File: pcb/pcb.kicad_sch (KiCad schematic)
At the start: 10 parts, among them J1 encoder, J2 programmer, J3 oled display, J4 usb-ttl, SW1 reset, U1 ATmega32-16P

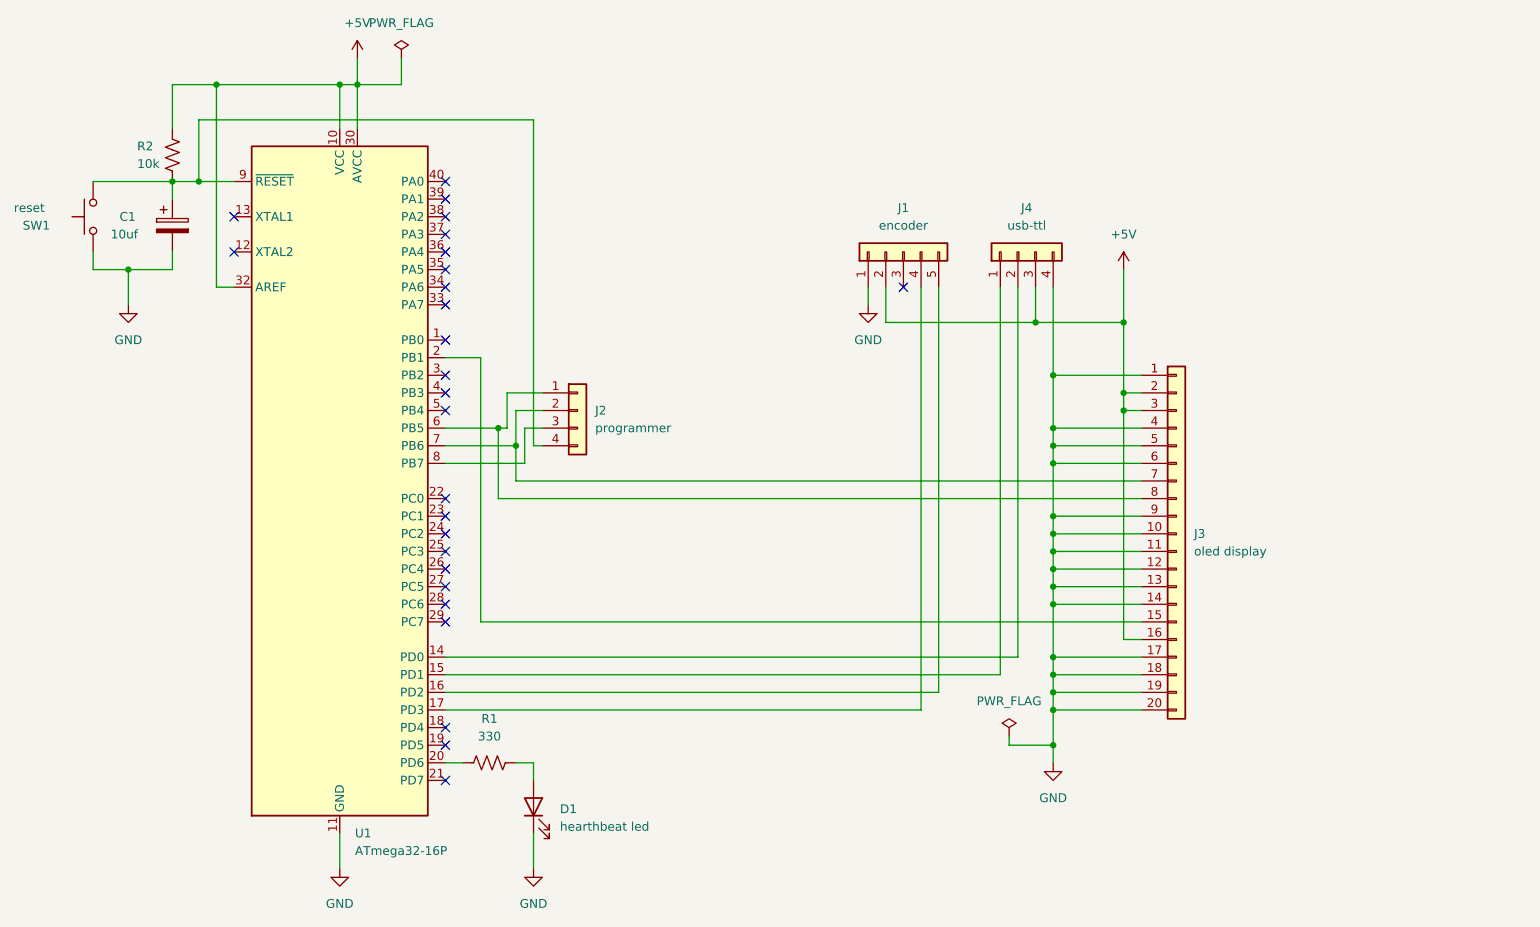
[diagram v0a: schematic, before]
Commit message: actualizo PCB con switches next, prev, play
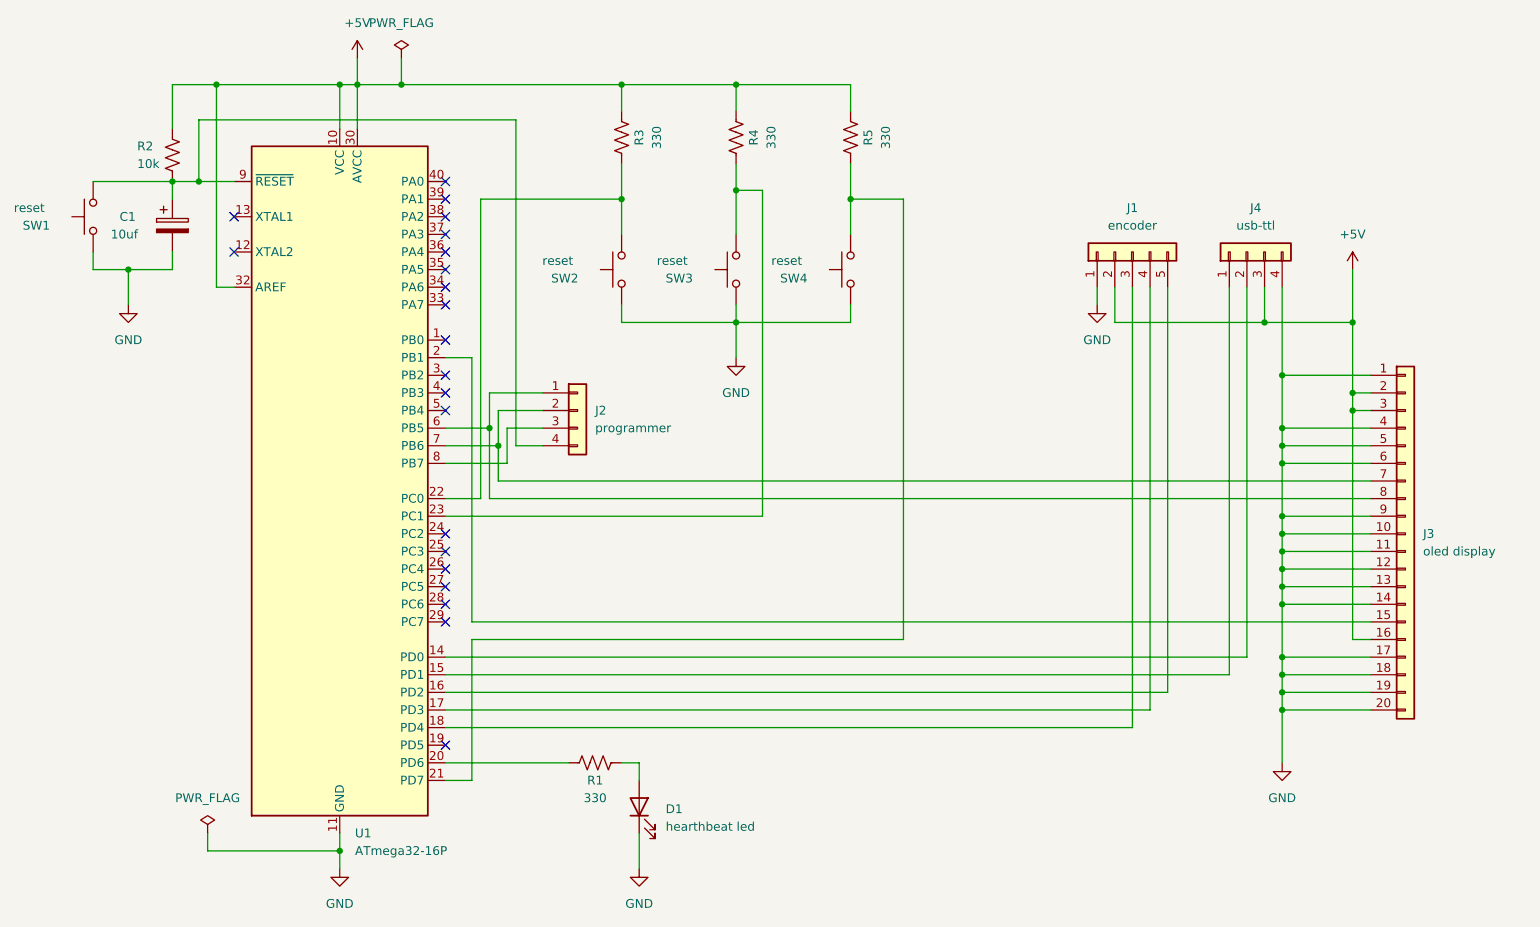
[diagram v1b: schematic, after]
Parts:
- added R3, R4, R5: 330, Resistor_THT:R_Axial_DIN0207_L6.3mm_D2.5mm_P7.62mm_Horizontal, symbol Device:R_US
- added SW2, SW3, SW4: reset, Button_Switch_THT:SW_PUSH_6mm, symbol Switch:SW_Push
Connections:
- net +5V: now also R3.2, R4.2, R5.2
- net GND: now also SW2.1, SW3.1, SW4.1
- net at U1.18 (PD4): now also J1.3 (Pin_3)
- net at U1.21 (PD7): now also R5.1, SW4.2
- net at U1.22 (PC0): now also R3.1, SW2.2
- net at U1.23 (PC1): now also R4.1, SW3.2
- no-connect marks 26 -> 21
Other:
- moved on the sheet: D1, J1, J3, J4, R1

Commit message: actualizacion de pcb
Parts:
- SW2: value reset -> play/pause
- SW3: value reset -> prev track
- SW4: value reset -> next track
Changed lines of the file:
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@@
       (effects (font (size 1.27 1.27)) (justify right))
     )
-    (property "Value" "reset" (at 177.8 68.58 90)
+    (property "Value" "next track" (at 177.8 68.58 90)
       (effects (font (size 1.27 1.27)) (justify right))
     )
@@
       (effects (font (size 1.27 1.27)) (justify right))
     )
-    (property "Value" "reset" (at 144.78 68.58 90)
+    (property "Value" "play/pause" (at 144.78 68.58 90)
       (effects (font (size 1.27 1.27)) (justify right))
     )
@@
       (effects (font (size 1.27 1.27)) (justify right))
     )
-    (property "Value" "reset" (at 161.29 68.58 90)
-      (effects (font (size 1.27 1.27)) (justify right))
-    )
+    (property "Value" "prev track" (at 161.29 68.58 90)
+      (effects (font (size 1.27 1.27)) (justify right))
+    )
